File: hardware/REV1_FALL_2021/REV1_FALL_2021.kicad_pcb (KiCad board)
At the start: 2 copper layers, 24 parts, among them J101 Screw_Terminal_01x02, Q101 Q_NMOS_GDS, U1 Teensy3.6_All_Pins, U2 PA16165_Breakout, U201 TPS2113ADRBR, U3 MPL3115A2_Breakout, U301 TPS2113ADRBR, U4 BNO055_Breakout, U5 RFM69HCW_Breakout

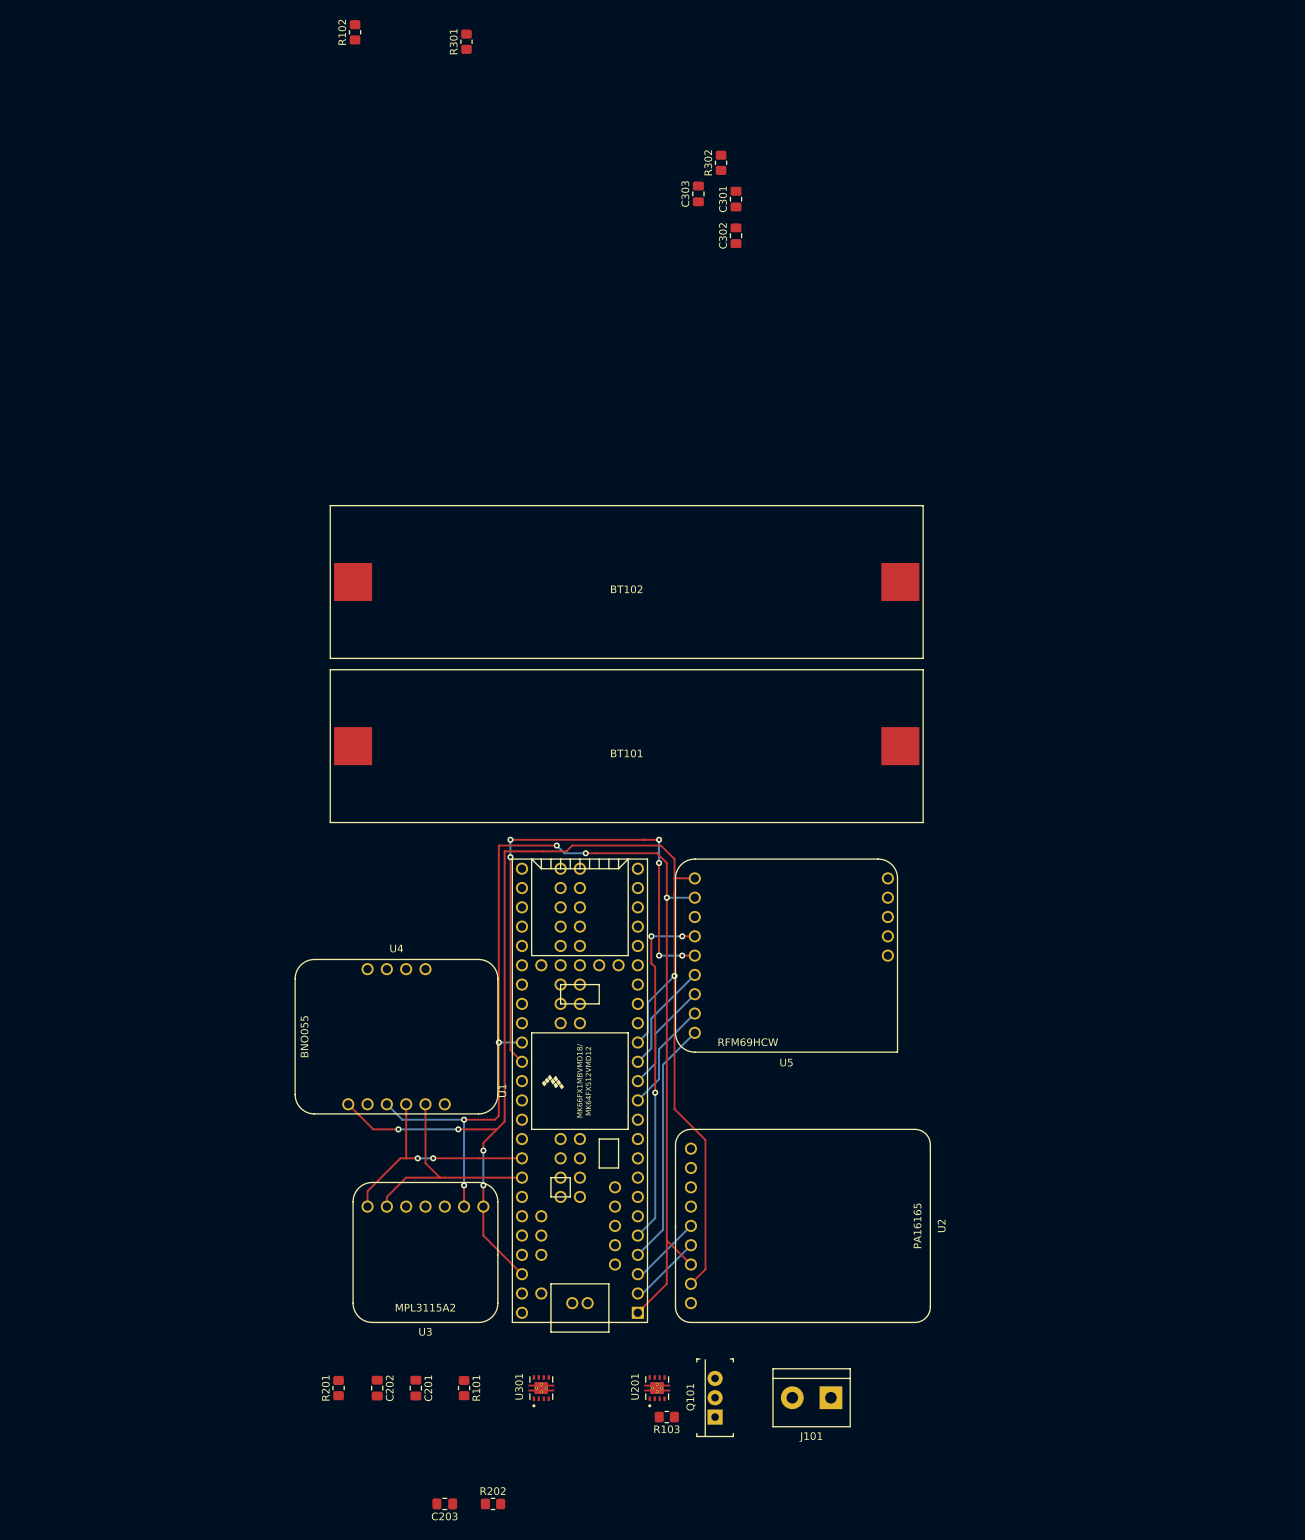
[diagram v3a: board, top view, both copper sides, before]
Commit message: layout mostly finished
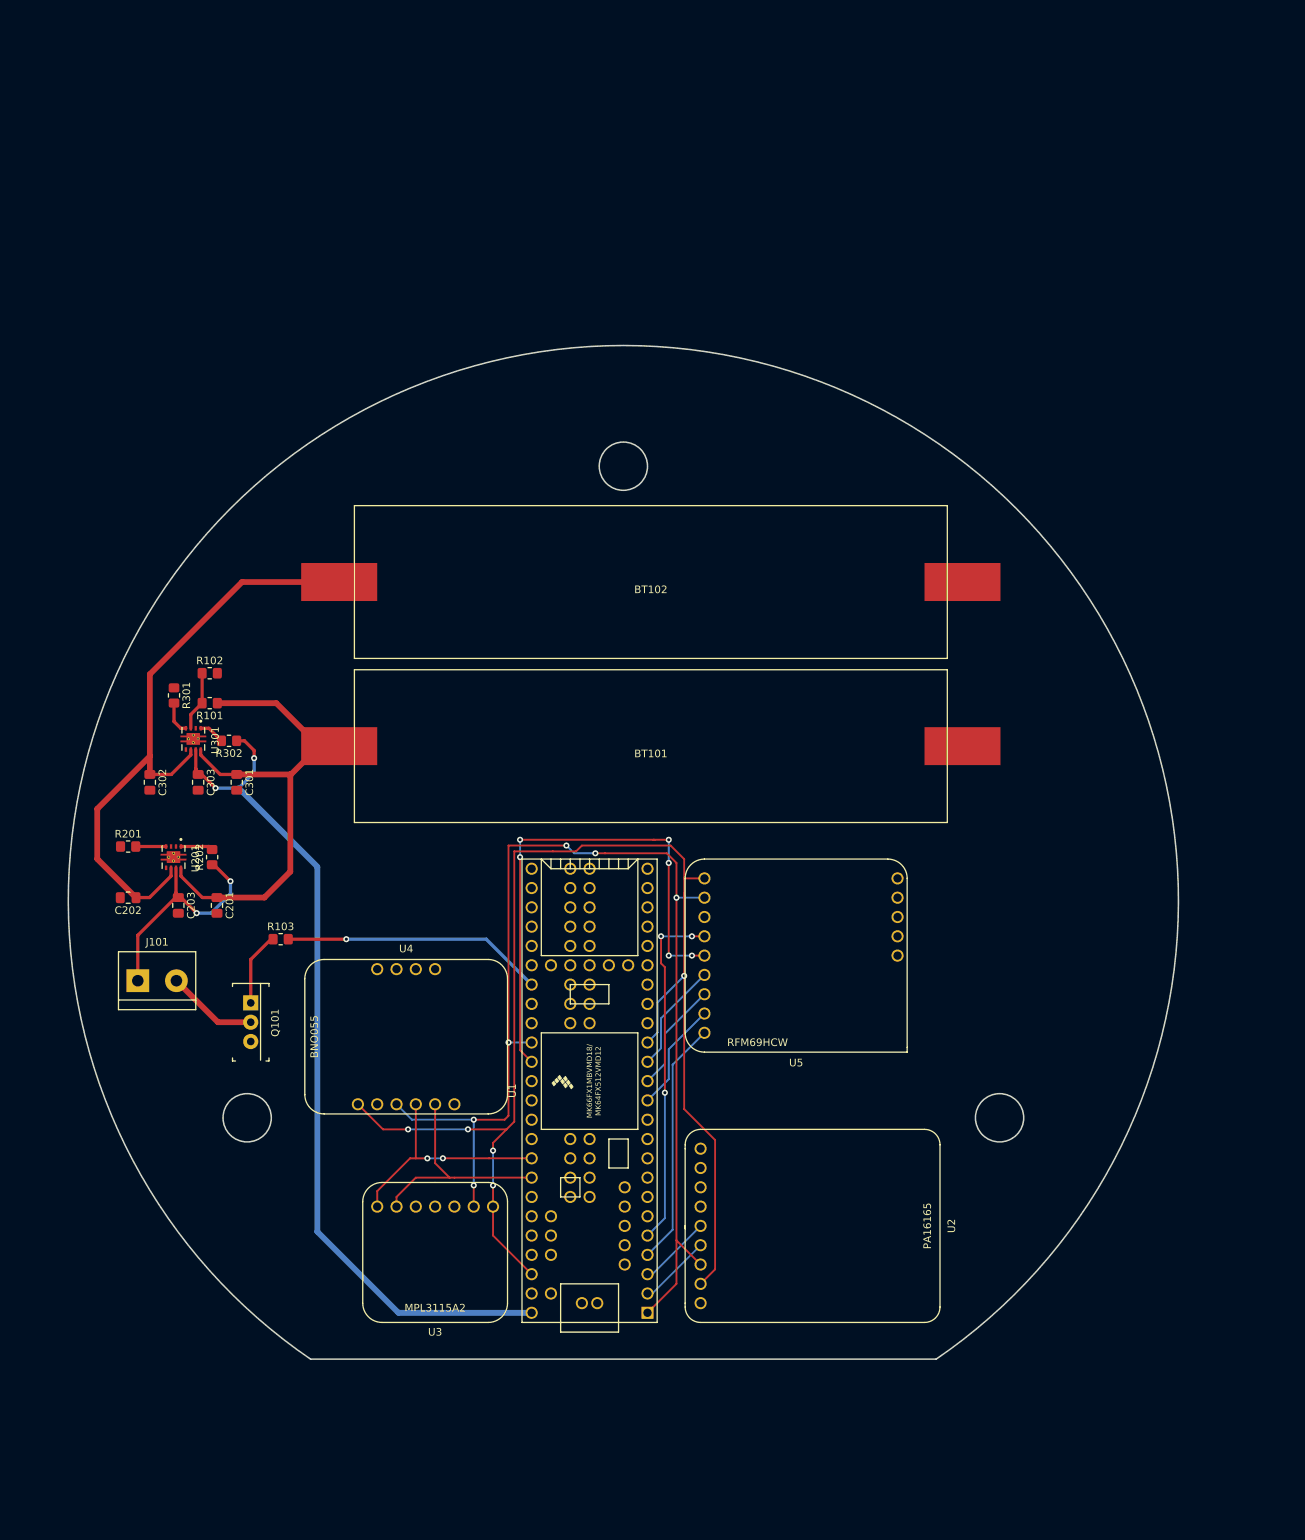
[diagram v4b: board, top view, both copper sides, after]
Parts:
- moved J101 106.4 mm to (36.4, 113.4), turned to 0 degrees
- moved C302 105.4 mm to (38.0, 87.3), turned to 270 degrees
- moved C303 101.6 mm to (44.4, 87.3), turned to 270 degrees
- moved C301 101.0 mm to (49.5, 87.3), turned to 270 degrees
- moved R302 99.9 mm to (48.5, 81.9), turned to 180 degrees
- moved U301 96.9 mm to (43.8, 81.6), turned to 270 degrees
- moved R101 96.1 mm to (45.9, 76.9), turned to 180 degrees
- moved U201 94.5 mm to (41.1, 97.2), turned to 270 degrees
- moved R301 94.2 mm to (41.2, 75.9), turned to 270 degrees
- moved R202 92.8 mm to (46.2, 97.2), turned to 90 degrees
- moved R102 86.5 mm to (45.9, 73.0), turned to 0 degrees
- moved C203 86.2 mm to (41.8, 103.5), turned to 270 degrees
- moved Q101 81.9 mm to (51.3, 116.3), turned to 270 degrees
- moved R103 80.8 mm to (55.2, 108.0), turned to 0 degrees
- moved R201 76.4 mm to (35.2, 95.8), turned to 0 degrees
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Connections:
- U1 pad 10: (no net) -> Net-(U1-Pad10)
- U1 pad 11: (no net) -> Net-(U1-Pad11)
- U1 pad 16: (no net) -> Net-(U1-Pad16)
- U1 pad 17: (no net) -> Net-(U1-Pad17)
- U1 pad 18: (no net) -> Net-(U1-Pad18)
- U1 pad 19: (no net) -> Net-(U1-Pad19)
- U1 pad 20: (no net) -> Net-(U1-Pad20)
- U1 pad 21: (no net) -> Net-(U1-Pad21)
- U1 pad 22: (no net) -> Net-(U1-Pad22)
- U1 pad 23: (no net) -> Net-(U1-Pad23)
- U1 pad 24: (no net) -> Net-(U1-Pad24)
- U1 pad 25: (no net) -> Net-(U1-Pad25)
- U1 pad 26: (no net) -> Net-(U1-Pad26)
- U1 pad 27: (no net) -> Net-(U1-Pad27)
- U1 pad 28: (no net) -> Net-(U1-Pad28)
- U1 pad 29: (no net) -> Net-(U1-Pad29)
- U1 pad 30: (no net) -> Net-(U1-Pad30)
- U1 pad 31: (no net) -> Net-(U1-Pad31)
- U1 pad 35: (no net) -> Net-(U1-Pad35)
- U1 pad 37: (no net) -> Net-(U1-Pad37)
- U1 pad 38: (no net) -> Net-(U1-Pad38)
- U1 pad 41: (no net) -> Net-(U1-Pad41)
- U1 pad 42: (no net) -> Net-(U1-Pad42)
- U1 pad 43: (no net) -> Net-(U1-Pad43)
- U1 pad 44: (no net) -> Net-(U1-Pad44)
- U1 pad 47: (no net) -> Net-(U1-Pad47)
- U1 pad 48: (no net) -> Net-(U1-Pad48)
- U1 pad 49: (no net) -> Net-(U1-Pad49)
- U1 pad 50: (no net) -> Net-(U1-Pad50)
- U1 pad 52: (no net) -> Net-(U1-Pad52)
- U1 pad 54: (no net) -> Net-(U1-Pad54)
- U1 pad 55: (no net) -> Net-(U1-Pad55)
- U1 pad 56: (no net) -> Net-(U1-Pad56)
- U1 pad 57: (no net) -> Net-(U1-Pad57)
- U1 pad 58: (no net) -> Net-(U1-Pad58)
- U1 pad 59: (no net) -> Net-(U1-Pad59)
- U1 pad 6: (no net) -> Net-(U1-Pad6)
- U1 pad 60: (no net) -> Net-(U1-Pad60)
- U1 pad 61: (no net) -> Net-(U1-Pad61)
- U1 pad 62: (no net) -> Net-(U1-Pad62)
- U1 pad 63: (no net) -> Net-(U1-Pad63)
- U1 pad 64: (no net) -> Net-(U1-Pad64)
- U1 pad 65: (no net) -> Net-(U1-Pad65)
- U1 pad 66: (no net) -> Net-(U1-Pad66)
- U1 pad 67: (no net) -> Net-(U1-Pad67)
- U1 pad 68: (no net) -> Net-(U1-Pad68)
- U1 pad 69: (no net) -> Net-(U1-Pad69)
- U1 pad 7: (no net) -> Net-(U1-Pad7)
- U1 pad 70: (no net) -> Net-(U1-Pad70)
- U1 pad 71: (no net) -> Net-(U1-Pad71)
- U1 pad 72: (no net) -> Net-(U1-Pad72)
- U1 pad 73: (no net) -> Net-(U1-Pad73)
- U1 pad 74: (no net) -> Net-(U1-Pad74)
- U1 pad 75: (no net) -> Net-(U1-Pad75)
- U1 pad 76: (no net) -> Net-(U1-Pad76)
- U1 pad 77: (no net) -> Net-(U1-Pad77)
- U1 pad 78: (no net) -> Net-(U1-Pad78)
- U1 pad 79: (no net) -> Net-(U1-Pad79)
- U1 pad 8: (no net) -> Net-(U1-Pad8)
- U1 pad 80: (no net) -> Net-(U1-Pad80)
- U1 pad 81: (no net) -> Net-(U1-Pad81)
- U1 pad 82: (no net) -> Net-(U1-Pad82)
- U1 pad 83: (no net) -> Net-(U1-Pad83)
- U1 pad 84: (no net) -> Net-(U1-Pad84)
- U1 pad 85: (no net) -> Net-(U1-Pad85)
- U1 pad 86: (no net) -> Net-(U1-Pad86)
- U1 pad 87: (no net) -> Net-(U1-Pad87)
- U1 pad 88: (no net) -> Net-(U1-Pad88)
- U1 pad 9: (no net) -> Net-(U1-Pad9)
- U2 pad 1: (no net) -> Net-(U2-Pad1)
- U2 pad 2: (no net) -> Net-(U2-Pad2)
- U2 pad 3: (no net) -> Net-(U2-Pad3)
- U2 pad 4: (no net) -> Net-(U2-Pad4)
- U2 pad 9: (no net) -> Net-(U2-Pad9)
- U3 pad 3: (no net) -> Net-(U3-Pad3)
- U3 pad 4: (no net) -> Net-(U3-Pad4)
- U3 pad 5: (no net) -> Net-(U3-Pad5)
- U4 pad 10: (no net) -> Net-(U4-Pad10)
- U4 pad 2: (no net) -> Net-(U4-Pad2)
- U4 pad 6: (no net) -> Net-(U4-Pad6)
- U4 pad 7: (no net) -> Net-(U4-Pad7)
- U4 pad 8: (no net) -> Net-(U4-Pad8)
- U4 pad 9: (no net) -> Net-(U4-Pad9)
- U5 pad 10: (no net) -> Net-(U5-Pad10)
- U5 pad 11: (no net) -> Net-(U5-Pad11)
- U5 pad 12: (no net) -> Net-(U5-Pad12)
- U5 pad 13: (no net) -> Net-(U5-Pad13)
- U5 pad 14: (no net) -> Net-(U5-Pad14)
- U5 pad 3: (no net) -> Net-(U5-Pad3)
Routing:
- net /V_TEENSY: track 0.00 -> 113.5 mm, vias 0 -> 2
- net /TPS2113A for E-match/IN2: track 0.00 -> 80.9 mm
- net /TPS2113A for E-match/IN1: track 0.00 -> 70.8 mm
- net /E-MATCH_TRIGGER: track 0.00 -> 34.5 mm, vias 0 -> 1
- net /V_EMATCH: track 0.00 -> 31.4 mm, vias 0 -> 2
- net Net-(J101-Pad2): track 0.00 -> 12.0 mm
- net Net-(Q101-Pad1): track 0.00 -> 9.76 mm
- net /TPS2113A for Teensy power/VSNS: track 0.00 -> 7.85 mm
- net Net-(R301-Pad2): track 0.00 -> 4.36 mm
- net /TPS_2_STAT: track 0.00 -> 4.27 mm
- net Net-(R201-Pad2): track 0.00 -> 4.00 mm
- net /TPS_1_STAT: track 0.00 -> 3.41 mm
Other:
- board outline added: 146 x 133.4 mm

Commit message: add filled zones
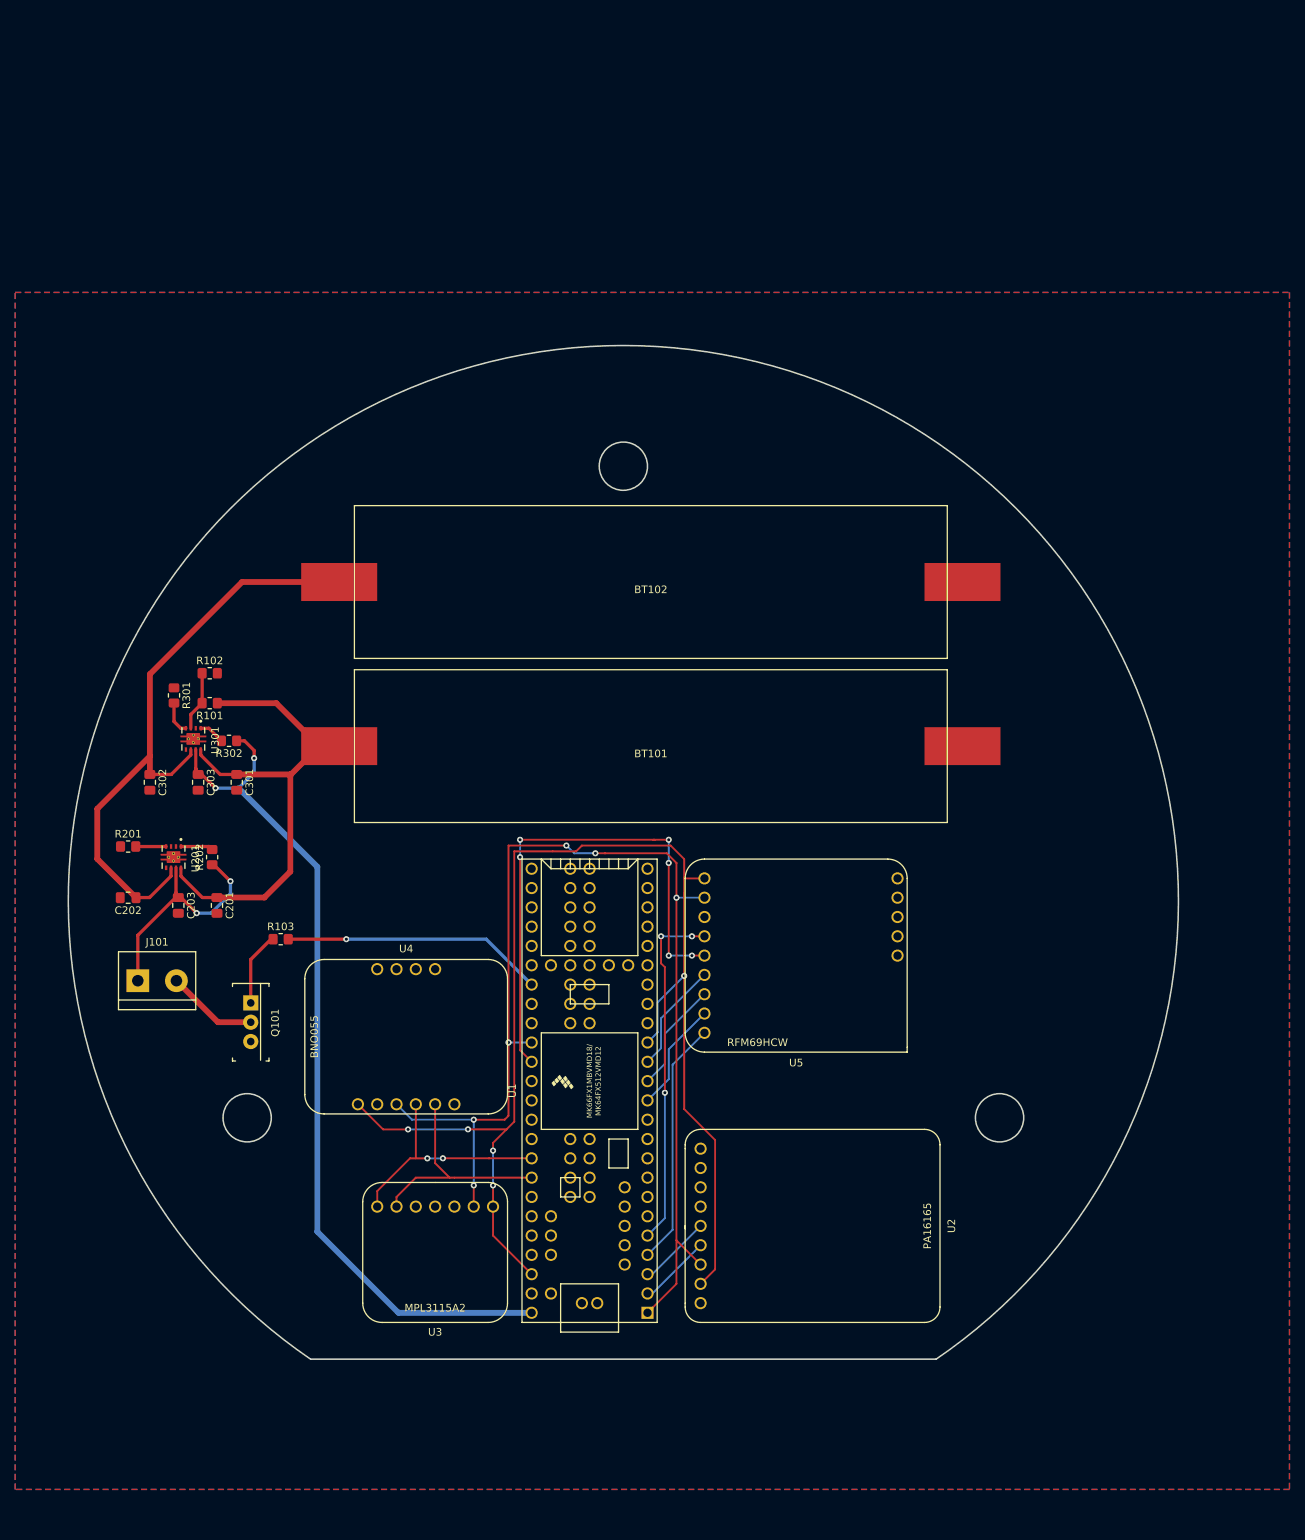
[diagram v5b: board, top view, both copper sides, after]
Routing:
- added copper zone on B.Cu, net GND
- added copper zone on F.Cu, net GND
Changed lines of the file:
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@@
   (segment (start 31.115 90.805) (end 31.115 97.3875) (width 0.762) (layer F.Cu) (net 114))
   (segment (start 38.0365 83.8835) (end 31.115 90.805) (width 0.762) (layer F.Cu) (net 114))
+  (zone (net 12) (net_name GND) (layer F.Cu) (hatch edge 0.508)
+    (connect_pads (clearance 0.25))
+    (min_thickness 0.24)
+    (fill yes (arc_segments 32) (thermal_gap 0.508) (thermal_bridge_width 0.508))
+    (polygon
+      (pts
+        (xy 20.32 22.86) (xy 187.96 22.86) (xy 187.96 180.34) (xy 20.32 180.34)
+      )
+    )
+  )
+  (zone (net 12) (net_name GND) (layer B.Cu) (hatch edge 0.508)
+    (connect_pads (clearance 0.25))
+    (min_thickness 0.24)
+    (fill yes (arc_segments 32) (thermal_gap 0.508) (thermal_bridge_width 0.508))
+    (polygon
+      (pts
+        (xy 20.32 22.86) (xy 187.96 22.86) (xy 187.96 180.34) (xy 20.32 180.34)
+      )
+    )
+  )
 )
